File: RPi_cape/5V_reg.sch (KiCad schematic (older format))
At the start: 18 parts, among them U34 LMZ14203

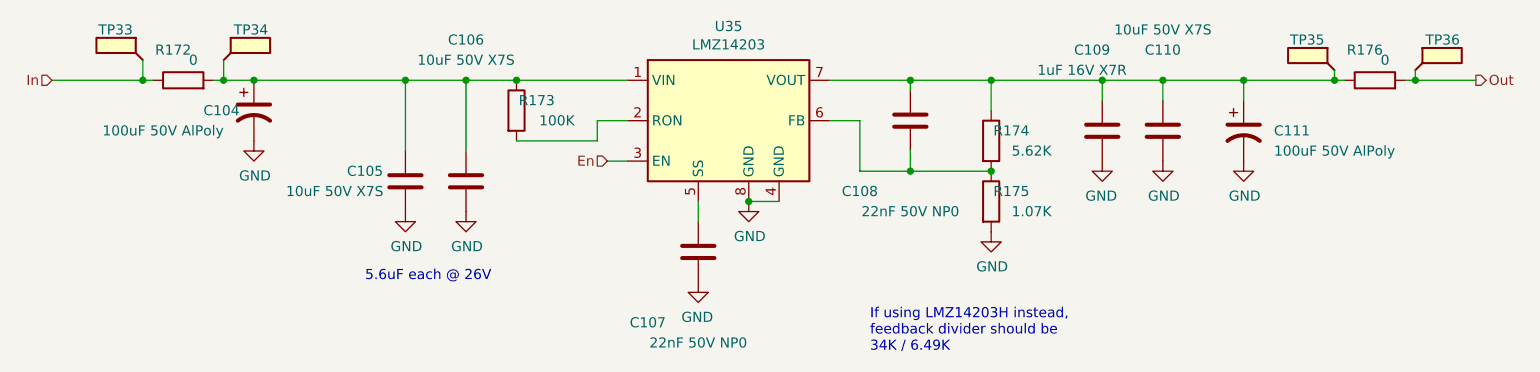
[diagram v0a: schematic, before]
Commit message: Extra info, post-design-review fixes
Added extra info on existing alternate circuit options
Added extra info on parts selection
Created initial PCB file
Added bulk cap to +5V input
Design review fixes:
Moved Raspberry Pi PWM output to GPIO18 to take advantage of hardware PWM
Fixed floating shutdown input on audio amp
Added series resistor R177 to allow low battery output to signal to both CPLD and external LED at the same time
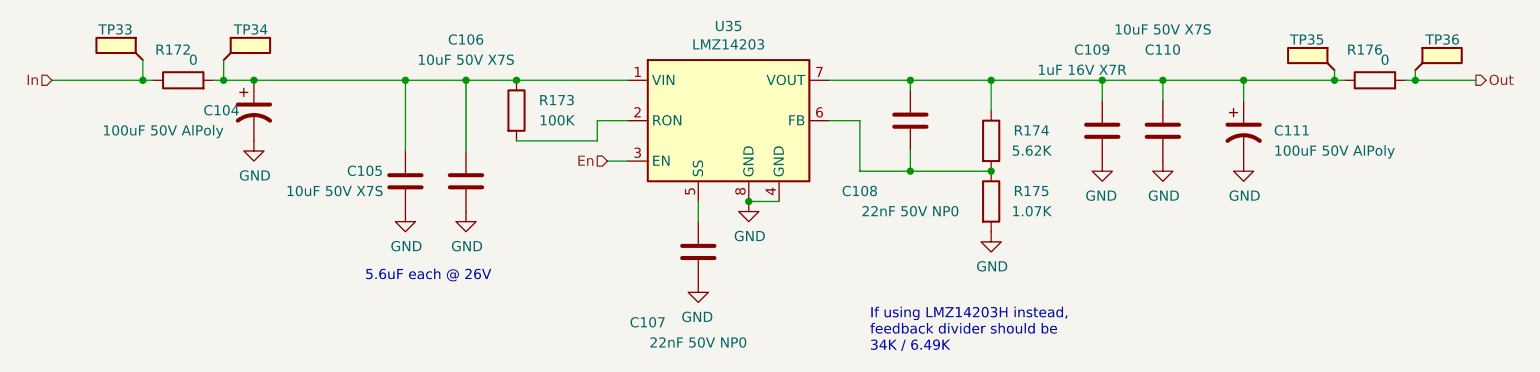
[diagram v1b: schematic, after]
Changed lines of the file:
@@
 AR Path="/5EE065CD/5EE14EEB" Ref="R169"  Part="1"
 AR Path="/5EEB3F52/5EE14EEB" Ref="R174"  Part="1"
-F 0 "R174" H 6400 3100 50  0000 C CNN
+F 0 "R174" H 6500 3100 50  0000 C CNN
 F 1 "5.62K" H 6500 3000 50  0000 C CNN
 F 2 "Resistor_SMD:R_1206_3216Metric" V 6230 3050 50  0001 C CNN
@@
 AR Path="/5EE065CD/5EE16CD0" Ref="R170"  Part="1"
 AR Path="/5EEB3F52/5EE16CD0" Ref="R175"  Part="1"
-F 0 "R175" H 6400 3400 50  0000 C CNN
+F 0 "R175" H 6500 3400 50  0000 C CNN
 F 1 "1.07K" H 6500 3300 50  0000 C CNN
 F 2 "Resistor_SMD:R_1206_3216Metric" V 6230 3350 50  0001 C CNN
@@
 AR Path="/5EE065CD/5EE170F2" Ref="R168"  Part="1"
 AR Path="/5EEB3F52/5EE170F2" Ref="R173"  Part="1"
-F 0 "R173" H 4050 2950 50  0000 C CNN
+F 0 "R173" H 4150 2950 50  0000 C CNN
 F 1 "100K" H 4150 2850 50  0000 C CNN
 F 2 "Resistor_SMD:R_1206_3216Metric" V 3880 2900 50  0001 C CNN

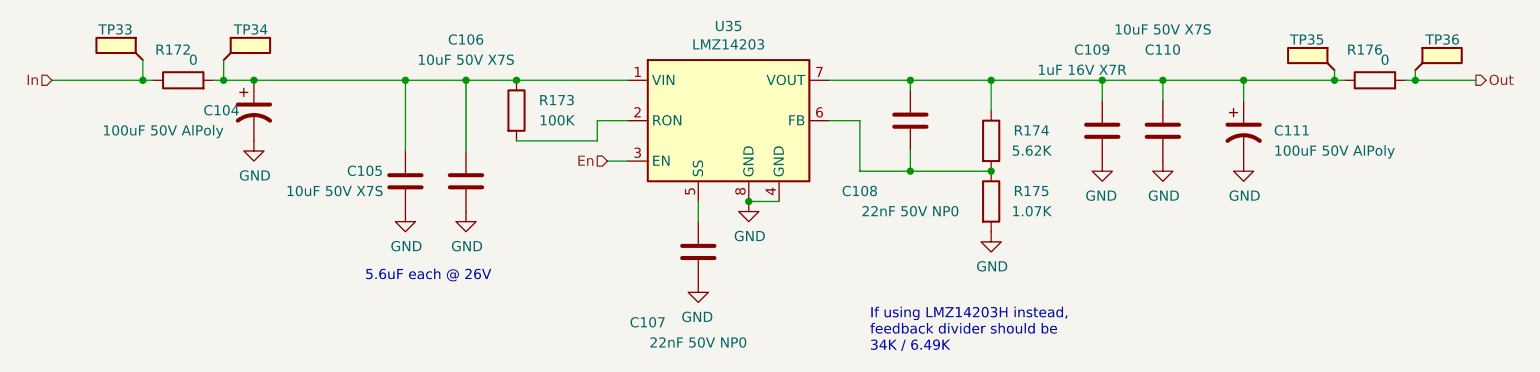
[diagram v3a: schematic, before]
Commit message: Better valve monitoring, finalized layout and manufacturing files
Created assembly and fabrication drawings, assigned all BOM parts, generally made design ready for ordering
Added strain-relief slots and barb mounting dimensions for digital pressure sensors
Changed valve drivers from discrete power MOSFETs to "smart" industrial/automotive driver ICs for the current monitoring, including valve-movement monitor for #4
Connected RPi_Valve* signals to larger CPLD footprint, changed Raspberry Pi pin assignment as a result to ease PCB routing
Updated footprints, page layout to create readable assembly drawing
Added current-measurement testpoints for CPLD power from BATT+
Changed power diodes in power-down-alarm circuit to small-signal parts for more compact layout
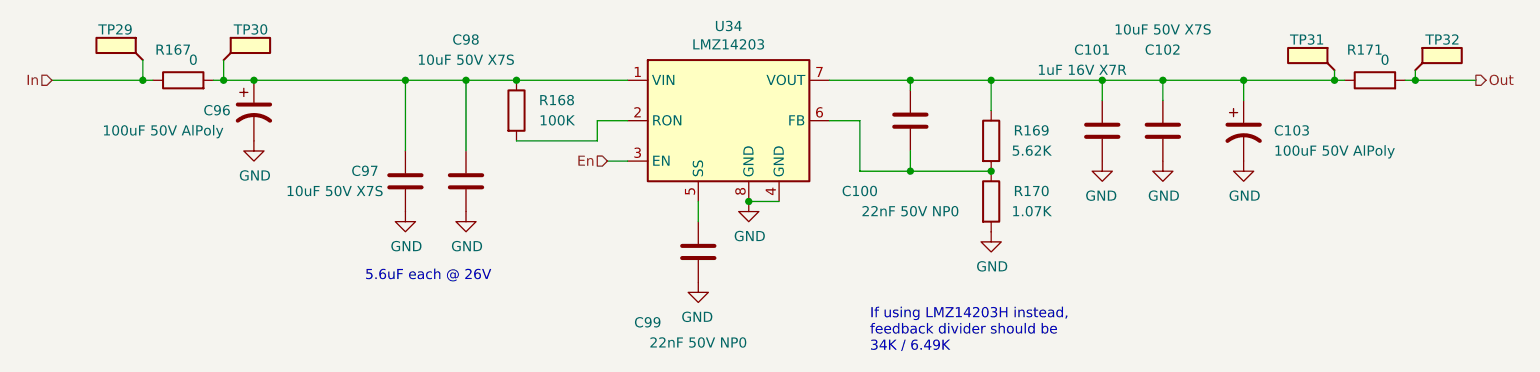
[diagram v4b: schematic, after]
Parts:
- R167, R171: Manufacturer (none) -> Panasonic; Part Number (none) -> ERJ-8GEY0R00V
- R168: Manufacturer (none) -> KOA Speer; Part Number (none) -> RK73H2BTTD1003F
- R169: Manufacturer (none) -> KOA Speer; Part Number (none) -> RK73H2BTTD5621F
- R170: Manufacturer (none) -> KOA Speer; Part Number (none) -> RK73H2BTTD1071F
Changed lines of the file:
@@
 $Descr A4 11693 8268
 encoding utf-8
-Sheet 11 14
+Sheet 11 15
 Title "5V Buck Regulator"
 Date ""
@@
 AR Path="/5EE065CD/5EE088D9" Ref="U34"  Part="1"
 AR Path="/5EEB3F52/5EE088D9" Ref="U35"  Part="1"
-F 0 "U35" H 5000 3417 50  0000 C CNN
+F 0 "U34" H 5000 3417 50  0000 C CNN
 F 1 "LMZ14203" H 5000 3326 50  0000 C CNN
 F 2 "Ventilator:TI_TO-PMOD-7" H 5000 2100 50  0001 C CNN
@@
 AR Path="/5EE065CD/5EE14EEB" Ref="R169"  Part="1"
 AR Path="/5EEB3F52/5EE14EEB" Ref="R174"  Part="1"
-F 0 "R174" H 6500 3100 50  0000 C CNN
+F 0 "R169" H 6500 3100 50  0000 C CNN
 F 1 "5.62K" H 6500 3000 50  0000 C CNN
 F 2 "Resistor_SMD:R_1206_3216Metric" V 6230 3050 50  0001 C CNN
 F 3 "~" H 6300 3050 50  0001 C CNN
+F 4 "KOA Speer" H 6300 3050 50  0001 C CNN "Manufacturer"
+F 5 "RK73H2BTTD5621F" H 6300 3050 50  0001 C CNN "Part Number"
 	1    6300 3050
 	1    0    0    -1
@@
 AR Path="/5EE065CD/5EE14EF1" Ref="C97"  Part="1"
 AR Path="/5EEB3F52/5EE14EF1" Ref="C105"  Part="1"
-F 0 "C105" H 3600 3300 50  0000 C CNN
+F 0 "C97" H 3600 3300 50  0000 C CNN
 F 1 "10uF 50V X7S" H 3750 3200 50  0000 C CNN
 F 2 "Capacitor_SMD:C_1210_3225Metric" H 3438 3100 50  0001 C CNN
@@
 AR Path="/5EE065CD/5EE16CD0" Ref="R170"  Part="1"
 AR Path="/5EEB3F52/5EE16CD0" Ref="R175"  Part="1"
-F 0 "R175" H 6500 3400 50  0000 C CNN
+F 0 "R170" H 6500 3400 50  0000 C CNN
 F 1 "1.07K" H 6500 3300 50  0000 C CNN
 F 2 "Resistor_SMD:R_1206_3216Metric" V 6230 3350 50  0001 C CNN
 F 3 "~" H 6300 3350 50  0001 C CNN
+F 4 "KOA Speer" H 6300 3350 50  0001 C CNN "Manufacturer"
+F 5 "RK73H2BTTD1071F" H 6300 3350 50  0001 C CNN "Part Number"
 	1    6300 3350
 	1    0    0    -1
@@
 AR Path="/5EE065CD/5EE170F2" Ref="R168"  Part="1"
 AR Path="/5EEB3F52/5EE170F2" Ref="R173"  Part="1"
-F 0 "R173" H 4150 2950 50  0000 C CNN
+F 0 "R168" H 4150 2950 50  0000 C CNN
 F 1 "100K" H 4150 2850 50  0000 C CNN
 F 2 "Resistor_SMD:R_1206_3216Metric" V 3880 2900 50  0001 C CNN
 F 3 "~" H 3950 2900 50  0001 C CNN
+F 4 "KOA Speer" H 3950 2900 50  0001 C CNN "Manufacturer"
+F 5 "RK73H2BTTD1003F" H 3950 2900 50  0001 C CNN "Part Number"
 	1    3950 2900
 	1    0    0    -1
@@
 AR Path="/5EE065CD/5EE2670E" Ref="C99"  Part="1"
 AR Path="/5EEB3F52/5EE2670E" Ref="C107"  Part="1"
-F 0 "C107" H 4600 3950 50  0000 C CNN
+F 0 "C99" H 4600 3950 50  0000 C CNN
 F 1 "22nF 50V NP0" H 4850 4050 50  0000 C CNN
 F 2 "Capacitor_SMD:C_0805_2012Metric" H 4888 3450 50  0001 C CNN
@@
 AR Path="/5EE065CD/5EE27BE3" Ref="C100"  Part="1"
 AR Path="/5EEB3F52/5EE27BE3" Ref="C108"  Part="1"
-F 0 "C108" H 5650 3300 50  0000 C CNN
+F 0 "C100" H 5650 3300 50  0000 C CNN
 F 1 "22nF 50V NP0" H 5900 3400 50  0000 C CNN
 F 2 "Capacitor_SMD:C_0805_2012Metric" H 5938 2800 50  0001 C CNN
@@
 AR Path="/5EE065CD/5EE2ABB7" Ref="C102"  Part="1"
 AR Path="/5EEB3F52/5EE2ABB7" Ref="C110"  Part="1"
-F 0 "C110" H 7150 3400 50  0000 C CNN
+F 0 "C102" H 7150 3400 50  0000 C CNN
 F 1 "10uF 50V X7S" H 7150 3500 50  0000 C CNN
 F 2 "Capacitor_SMD:C_1210_3225Metric" H 7188 2850 50  0001 C CNN
@@
 AR Path="/5EE065CD/5EE35666" Ref="C96"  Part="1"
 AR Path="/5EEB3F52/5EE35666" Ref="C104"  Part="1"
-F 0 "C104" H 2400 2900 50  0000 L CNN
+F 0 "C96" H 2400 2900 50  0000 L CNN
 F 1 "100uF 50V AlPoly" H 1900 2800 50  0000 L CNN
 F 2 "Capacitor_SMD:CP_Elec_10x10.5" H 2650 2900 50  0001 C CNN
@@
 AR Path="/5EE065CD/5EE38A1F" Ref="C103"  Part="1"
 AR Path="/5EEB3F52/5EE38A1F" Ref="C111"  Part="1"
-F 0 "C111" H 7700 3000 50  0000 L CNN
+F 0 "C103" H 7700 3000 50  0000 L CNN
 F 1 "100uF 50V AlPoly" H 7700 2900 50  0000 L CNN
 F 2 "Capacitor_SMD:CP_Elec_10x10.5" H 7550 3000 50  0001 C CNN
@@
 AR Path="/5EE065CD/5EE41F60" Ref="C101"  Part="1"
 AR Path="/5EEB3F52/5EE41F60" Ref="C109"  Part="1"
-F 0 "C109" H 6800 2600 50  0000 C CNN
+F 0 "C101" H 6800 2600 50  0000 C CNN
 F 1 "1uF 16V X7R" H 6750 2700 50  0000 C CNN
 F 2 "Capacitor_SMD:C_0805_2012Metric" H 6888 2850 50  0001 C CNN
@@
 AR Path="/5EE065CD/5EE4C23D" Ref="R171"  Part="1"
 AR Path="/5EEB3F52/5EE4C23D" Ref="R176"  Part="1"
-F 0 "R176" V 8350 2800 50  0000 C CNN
+F 0 "R171" V 8350 2800 50  0000 C CNN
 F 1 "0" V 8300 2700 50  0000 C CNN
 F 2 "Resistor_SMD:R_1206_3216Metric" V 8130 2750 50  0001 C CNN
 F 3 "~" H 8200 2750 50  0001 C CNN
+F 4 "Panasonic" H 8200 2750 50  0001 C CNN "Manufacturer"
+F 5 "ERJ-8GEY0R00V" H 8200 2750 50  0001 C CNN "Part Number"
 	1    8200 2750
 	0    -1   -1   0
@@
 AR Path="/5EE065CD/5EE50890" Ref="R167"  Part="1"
 AR Path="/5EEB3F52/5EE50890" Ref="R172"  Part="1"
-F 0 "R172" V 2450 2800 50  0000 C CNN
+F 0 "R167" V 2450 2800 50  0000 C CNN
 F 1 "0" V 2400 2700 50  0000 C CNN
 F 2 "Resistor_SMD:R_1206_3216Metric" V 2230 2750 50  0001 C CNN
 F 3 "~" H 2300 2750 50  0001 C CNN
+F 4 "Panasonic" H 2300 2750 50  0001 C CNN "Manufacturer"
+F 5 "ERJ-8GEY0R00V" H 2300 2750 50  0001 C CNN "Part Number"
 	1    2300 2750
 	0    -1   -1   0
@@
 AR Path="/5EE065CD/5EEA6827" Ref="TP30"  Part="1"
 AR Path="/5EEB3F52/5EEA6827" Ref="TP34"  Part="1"
-F 0 "TP34" H 2550 2800 50  0000 L CNN
+F 0 "TP30" H 2550 2800 50  0000 L CNN
 F 1 "TestPoint_Flag" H 2760 2653 50  0001 L CNN
 F 2 "TestPoint:TestPoint_Keystone_5019_Minature" H 2700 2650 50  0001 C CNN
@@
 AR Path="/5EE065CD/5EEA7A58" Ref="TP29"  Part="1"
 AR Path="/5EEB3F52/5EEA7A58" Ref="TP33"  Part="1"
-F 0 "TP33" H 2150 2800 50  0000 L CNN
+F 0 "TP29" H 2150 2800 50  0000 L CNN
 F 1 "TestPoint_Flag" H 2360 2653 50  0001 L CNN
 F 2 "TestPoint:TestPoint_Keystone_5019_Minature" H 2300 2650 50  0001 C CNN
@@
 AR Path="/5EE065CD/5EEA8BCB" Ref="TP31"  Part="1"
 AR Path="/5EEB3F52/5EEA8BCB" Ref="TP35"  Part="1"
-F 0 "TP35" H 8050 2850 50  0000 L CNN
+F 0 "TP31" H 8050 2850 50  0000 L CNN
 F 1 "TestPoint_Flag" H 8260 2703 50  0001 L CNN
 F 2 "TestPoint:TestPoint_Keystone_5019_Minature" H 8200 2700 50  0001 C CNN
@@
 AR Path="/5EE065CD/5EEAED2A" Ref="TP32"  Part="1"
 AR Path="/5EEB3F52/5EEAED2A" Ref="TP36"  Part="1"
-F 0 "TP36" H 8450 2850 50  0000 L CNN
+F 0 "TP32" H 8450 2850 50  0000 L CNN
 F 1 "TestPoint_Flag" H 8660 2703 50  0001 L CNN
 F 2 "TestPoint:TestPoint_Keystone_5019_Minature" H 8600 2700 50  0001 C CNN
@@
 AR Path="/5EE065CD/5F025002" Ref="C98"  Part="1"
 AR Path="/5EEB3F52/5F025002" Ref="C106"  Part="1"
-F 0 "C106" H 3700 3950 50  0000 C CNN
+F 0 "C98" H 3700 3950 50  0000 C CNN
 F 1 "10uF 50V X7S" H 3700 3850 50  0000 C CNN
 F 2 "Capacitor_SMD:C_1210_3225Metric" H 3738 3100 50  0001 C CNN

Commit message: Safety additions
Switched CPLD_ADC7 to +24V monitoring (from +5V monitoring), and added CPLD ~Bat_On digital input(s) to know when it's running from backup battery, to cover low-input-voltage edge cases
Added series 1K resistors (R226-231) on CPLD<->RPi Comms1-6 lines, to protect CPLD in case of overvoltage from RPi failure
Added optional input TVS D23 to handle sustained over-voltage or large surges
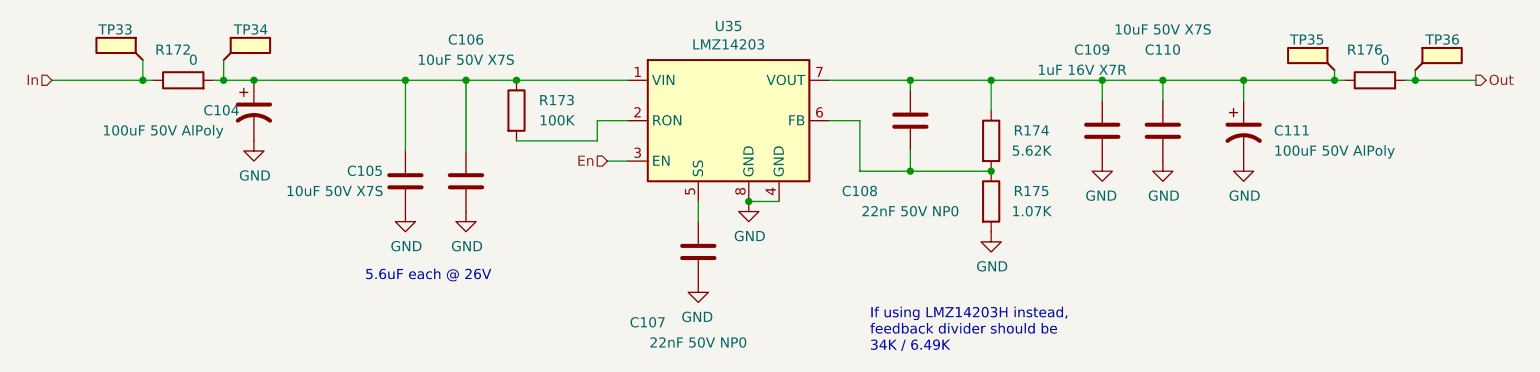
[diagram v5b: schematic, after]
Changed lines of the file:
@@
 AR Path="/5EE065CD/5EE088D9" Ref="U34"  Part="1"
 AR Path="/5EEB3F52/5EE088D9" Ref="U35"  Part="1"
-F 0 "U34" H 5000 3417 50  0000 C CNN
+F 0 "U35" H 5000 3417 50  0000 C CNN
 F 1 "LMZ14203" H 5000 3326 50  0000 C CNN
 F 2 "Ventilator:TI_TO-PMOD-7" H 5000 2100 50  0001 C CNN
@@
 AR Path="/5EE065CD/5EE14EEB" Ref="R169"  Part="1"
 AR Path="/5EEB3F52/5EE14EEB" Ref="R174"  Part="1"
-F 0 "R169" H 6500 3100 50  0000 C CNN
+F 0 "R174" H 6500 3100 50  0000 C CNN
 F 1 "5.62K" H 6500 3000 50  0000 C CNN
 F 2 "Resistor_SMD:R_1206_3216Metric" V 6230 3050 50  0001 C CNN
@@
 AR Path="/5EE065CD/5EE14EF1" Ref="C97"  Part="1"
 AR Path="/5EEB3F52/5EE14EF1" Ref="C105"  Part="1"
-F 0 "C97" H 3600 3300 50  0000 C CNN
+F 0 "C105" H 3600 3300 50  0000 C CNN
 F 1 "10uF 50V X7S" H 3750 3200 50  0000 C CNN
 F 2 "Capacitor_SMD:C_1210_3225Metric" H 3438 3100 50  0001 C CNN
@@
 AR Path="/5EE065CD/5EE16CD0" Ref="R170"  Part="1"
 AR Path="/5EEB3F52/5EE16CD0" Ref="R175"  Part="1"
-F 0 "R170" H 6500 3400 50  0000 C CNN
+F 0 "R175" H 6500 3400 50  0000 C CNN
 F 1 "1.07K" H 6500 3300 50  0000 C CNN
 F 2 "Resistor_SMD:R_1206_3216Metric" V 6230 3350 50  0001 C CNN
@@
 AR Path="/5EE065CD/5EE170F2" Ref="R168"  Part="1"
 AR Path="/5EEB3F52/5EE170F2" Ref="R173"  Part="1"
-F 0 "R168" H 4150 2950 50  0000 C CNN
+F 0 "R173" H 4150 2950 50  0000 C CNN
 F 1 "100K" H 4150 2850 50  0000 C CNN
 F 2 "Resistor_SMD:R_1206_3216Metric" V 3880 2900 50  0001 C CNN
@@
 AR Path="/5EE065CD/5EE2670E" Ref="C99"  Part="1"
 AR Path="/5EEB3F52/5EE2670E" Ref="C107"  Part="1"
-F 0 "C99" H 4600 3950 50  0000 C CNN
+F 0 "C107" H 4600 3950 50  0000 C CNN
 F 1 "22nF 50V NP0" H 4850 4050 50  0000 C CNN
 F 2 "Capacitor_SMD:C_0805_2012Metric" H 4888 3450 50  0001 C CNN
@@
 AR Path="/5EE065CD/5EE27BE3" Ref="C100"  Part="1"
 AR Path="/5EEB3F52/5EE27BE3" Ref="C108"  Part="1"
-F 0 "C100" H 5650 3300 50  0000 C CNN
+F 0 "C108" H 5650 3300 50  0000 C CNN
 F 1 "22nF 50V NP0" H 5900 3400 50  0000 C CNN
 F 2 "Capacitor_SMD:C_0805_2012Metric" H 5938 2800 50  0001 C CNN
@@
 AR Path="/5EE065CD/5EE2ABB7" Ref="C102"  Part="1"
 AR Path="/5EEB3F52/5EE2ABB7" Ref="C110"  Part="1"
-F 0 "C102" H 7150 3400 50  0000 C CNN
+F 0 "C110" H 7150 3400 50  0000 C CNN
 F 1 "10uF 50V X7S" H 7150 3500 50  0000 C CNN
 F 2 "Capacitor_SMD:C_1210_3225Metric" H 7188 2850 50  0001 C CNN
@@
 AR Path="/5EE065CD/5EE35666" Ref="C96"  Part="1"
 AR Path="/5EEB3F52/5EE35666" Ref="C104"  Part="1"
-F 0 "C96" H 2400 2900 50  0000 L CNN
+F 0 "C104" H 2400 2900 50  0000 L CNN
 F 1 "100uF 50V AlPoly" H 1900 2800 50  0000 L CNN
 F 2 "Capacitor_SMD:CP_Elec_10x10.5" H 2650 2900 50  0001 C CNN
@@
 AR Path="/5EE065CD/5EE38A1F" Ref="C103"  Part="1"
 AR Path="/5EEB3F52/5EE38A1F" Ref="C111"  Part="1"
-F 0 "C103" H 7700 3000 50  0000 L CNN
+F 0 "C111" H 7700 3000 50  0000 L CNN
 F 1 "100uF 50V AlPoly" H 7700 2900 50  0000 L CNN
 F 2 "Capacitor_SMD:CP_Elec_10x10.5" H 7550 3000 50  0001 C CNN
@@
 AR Path="/5EE065CD/5EE41F60" Ref="C101"  Part="1"
 AR Path="/5EEB3F52/5EE41F60" Ref="C109"  Part="1"
-F 0 "C101" H 6800 2600 50  0000 C CNN
+F 0 "C109" H 6800 2600 50  0000 C CNN
 F 1 "1uF 16V X7R" H 6750 2700 50  0000 C CNN
 F 2 "Capacitor_SMD:C_0805_2012Metric" H 6888 2850 50  0001 C CNN
@@
 AR Path="/5EE065CD/5EE4C23D" Ref="R171"  Part="1"
 AR Path="/5EEB3F52/5EE4C23D" Ref="R176"  Part="1"
-F 0 "R171" V 8350 2800 50  0000 C CNN
+F 0 "R176" V 8350 2800 50  0000 C CNN
 F 1 "0" V 8300 2700 50  0000 C CNN
 F 2 "Resistor_SMD:R_1206_3216Metric" V 8130 2750 50  0001 C CNN
@@
 AR Path="/5EE065CD/5EE50890" Ref="R167"  Part="1"
 AR Path="/5EEB3F52/5EE50890" Ref="R172"  Part="1"
-F 0 "R167" V 2450 2800 50  0000 C CNN
+F 0 "R172" V 2450 2800 50  0000 C CNN
 F 1 "0" V 2400 2700 50  0000 C CNN
 F 2 "Resistor_SMD:R_1206_3216Metric" V 2230 2750 50  0001 C CNN
@@
 AR Path="/5EE065CD/5EEA6827" Ref="TP30"  Part="1"
 AR Path="/5EEB3F52/5EEA6827" Ref="TP34"  Part="1"
-F 0 "TP30" H 2550 2800 50  0000 L CNN
+F 0 "TP34" H 2550 2800 50  0000 L CNN
 F 1 "TestPoint_Flag" H 2760 2653 50  0001 L CNN
 F 2 "TestPoint:TestPoint_Keystone_5019_Minature" H 2700 2650 50  0001 C CNN
@@
 AR Path="/5EE065CD/5EEA7A58" Ref="TP29"  Part="1"
 AR Path="/5EEB3F52/5EEA7A58" Ref="TP33"  Part="1"
-F 0 "TP29" H 2150 2800 50  0000 L CNN
+F 0 "TP33" H 2150 2800 50  0000 L CNN
 F 1 "TestPoint_Flag" H 2360 2653 50  0001 L CNN
 F 2 "TestPoint:TestPoint_Keystone_5019_Minature" H 2300 2650 50  0001 C CNN
@@
 AR Path="/5EE065CD/5EEA8BCB" Ref="TP31"  Part="1"
 AR Path="/5EEB3F52/5EEA8BCB" Ref="TP35"  Part="1"
-F 0 "TP31" H 8050 2850 50  0000 L CNN
+F 0 "TP35" H 8050 2850 50  0000 L CNN
 F 1 "TestPoint_Flag" H 8260 2703 50  0001 L CNN
 F 2 "TestPoint:TestPoint_Keystone_5019_Minature" H 8200 2700 50  0001 C CNN
@@
 AR Path="/5EE065CD/5EEAED2A" Ref="TP32"  Part="1"
 AR Path="/5EEB3F52/5EEAED2A" Ref="TP36"  Part="1"
-F 0 "TP32" H 8450 2850 50  0000 L CNN
+F 0 "TP36" H 8450 2850 50  0000 L CNN
 F 1 "TestPoint_Flag" H 8660 2703 50  0001 L CNN
 F 2 "TestPoint:TestPoint_Keystone_5019_Minature" H 8600 2700 50  0001 C CNN
@@
 AR Path="/5EE065CD/5F025002" Ref="C98"  Part="1"
 AR Path="/5EEB3F52/5F025002" Ref="C106"  Part="1"
-F 0 "C98" H 3700 3950 50  0000 C CNN
+F 0 "C106" H 3700 3950 50  0000 C CNN
 F 1 "10uF 50V X7S" H 3700 3850 50  0000 C CNN
 F 2 "Capacitor_SMD:C_1210_3225Metric" H 3738 3100 50  0001 C CNN

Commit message: Docs cleanup
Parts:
- C102, C97, C98: Part Number GCM32EC71H106KA03 -> GCM32EC71H106KA03L
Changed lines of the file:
@@
 F 3 "~" H 3400 3250 50  0001 C CNN
 F 4 "Murata" H 3400 3250 50  0001 C CNN "Manufacturer"
-F 5 "GCM32EC71H106KA03" H 3400 3250 50  0001 C CNN "Part Number"
+F 5 "GCM32EC71H106KA03L" H 3400 3250 50  0001 C CNN "Part Number"
 	1    3400 3250
 	-1   0    0    -1
@@
 F 3 "~" H 7150 3000 50  0001 C CNN
 F 4 "Murata" H 7150 3000 50  0001 C CNN "Manufacturer"
-F 5 "GCM32EC71H106KA03" H 7150 3000 50  0001 C CNN "Part Number"
+F 5 "GCM32EC71H106KA03L" H 7150 3000 50  0001 C CNN "Part Number"
 	1    7150 3000
 	-1   0    0    -1
@@
 F 3 "~" H 3700 3250 50  0001 C CNN
 F 4 "Murata" H 3700 3250 50  0001 C CNN "Manufacturer"
-F 5 "GCM32EC71H106KA03" H 3700 3250 50  0001 C CNN "Part Number"
+F 5 "GCM32EC71H106KA03L" H 3700 3250 50  0001 C CNN "Part Number"
 	1    3700 3250
 	-1   0    0    -1
